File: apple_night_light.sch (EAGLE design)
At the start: 46 parts, among them Y1 16MHZ, Y2 16mhz

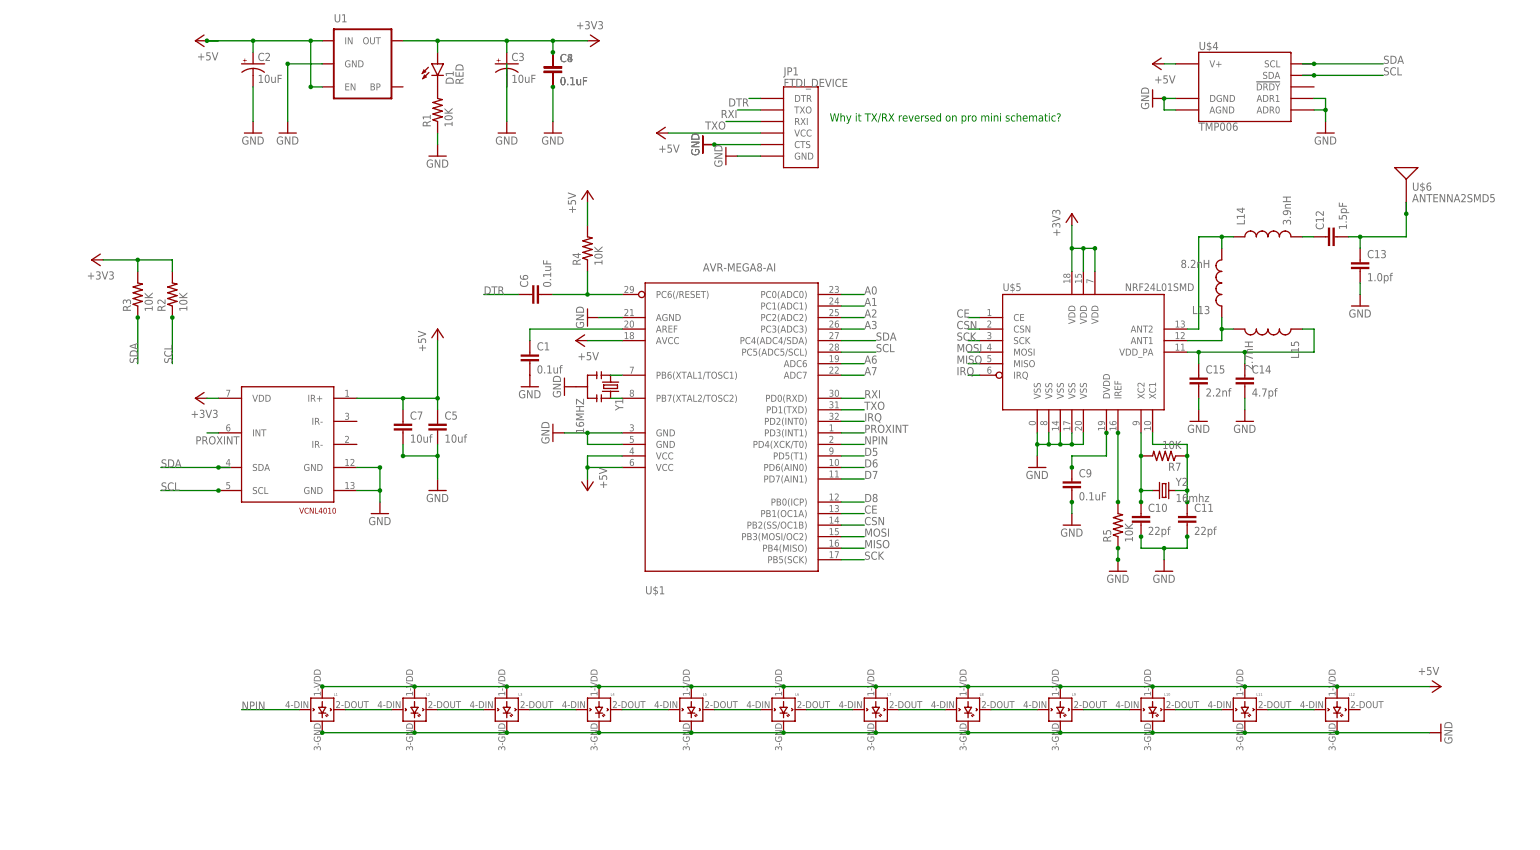
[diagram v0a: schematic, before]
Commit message: some routing, adding current sensor, ground pours
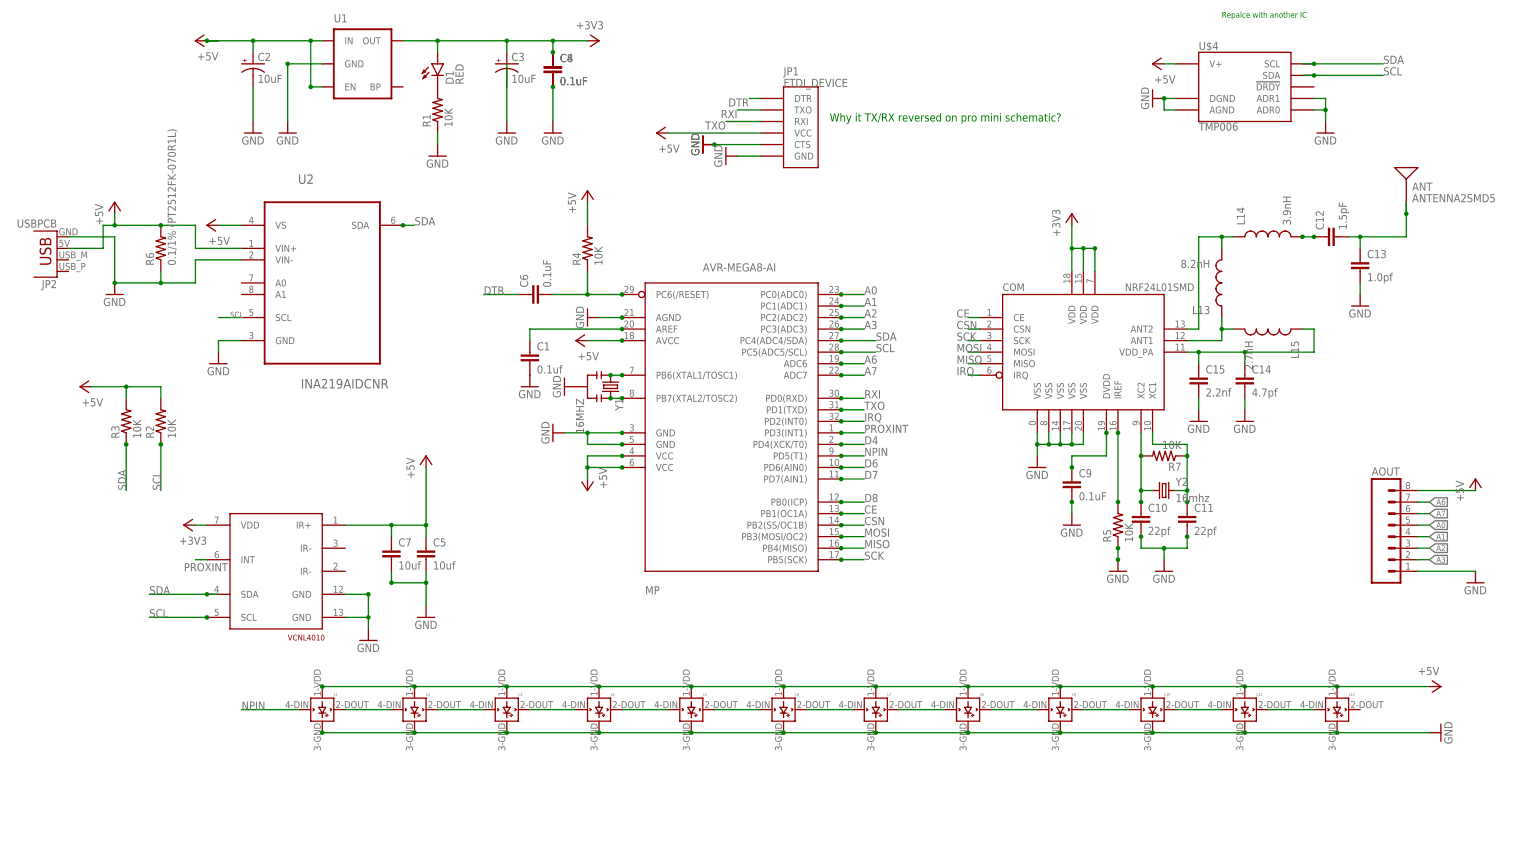
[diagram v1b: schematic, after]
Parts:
- added AOUT: (no value), SparkFun-Connectors:M08NO_SILK
- added JP2: USBPCB, SparkFun-Connectors:USBPCB
- added R6: 0.1/1% (PT2512FK-070R1L), SparkFun-Resistors:RESISTOR2512
- added U2: INA219AIDCNR, Texas Instruments_By_element14_Batch_1:INA219AIDCNR
- renumbered U$1 to MP, U$5 to COM, U$6 to ANT
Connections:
- removed net D5: MP.PD5(T1)
- new net D4: MP.PD4(XCK/T0)
- net +3V3: no longer R2.2, R3.2
- net +5V: now also AOUT.8, JP2.VBUS, R2.2, R3.2, R6.2, U2.VIN+, U2.VS
- net A0: now also AOUT.5
- net A1: now also AOUT.4
- net A2: now also AOUT.3
- net A3: now also AOUT.2
- net A6: now also AOUT.7
- net A7: now also AOUT.6
- net GND: now also AOUT.1, JP2.GND, R6.1, U2.GND, U2.VIN-
- net NPIN: now also MP.PD5(T1); no longer MP.PD4(XCK/T0)
- net PROXINT: now also MP.PD3(INT1)
- net SCL: now also U2.SCL
- net SDA: now also MP.PC4(ADC4/SDA), U2.SDA
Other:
- note added: "Repalce with another IC"
- moved on the sheet: C5, C7, R2, R3

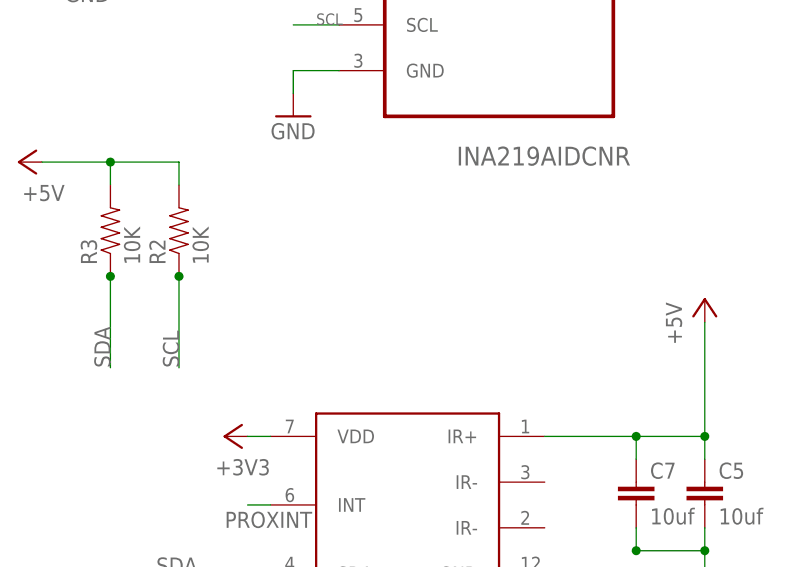
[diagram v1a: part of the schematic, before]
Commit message: usb passthrough placed, better routing on neopixel power
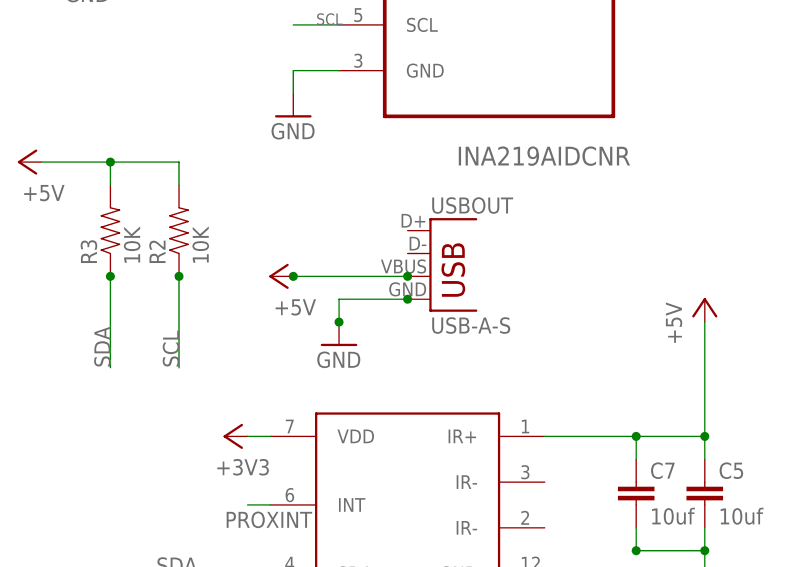
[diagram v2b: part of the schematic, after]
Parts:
- added USBOUT: USB-A-S, SparkFun-Connectors:USB-A-S
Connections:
- net +5V: now also USBOUT.VBUS
- net GND: now also USBOUT.GND
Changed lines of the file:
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@@
 <part name="P+12" library="supply1" deviceset="+5V" device=""/>
 <part name="GND27" library="supply1" deviceset="GND" device=""/>
+<part name="USBOUT" library="SparkFun-Connectors" deviceset="USB" device="-A-S"/>
+<part name="P+13" library="supply1" deviceset="+5V" device=""/>
+<part name="GND28" library="supply1" deviceset="GND" device=""/>
 </parts>
 <sheets>
@@
 <instance part="P+12" gate="1" x="-132.08" y="104.14"/>
 <instance part="GND27" gate="1" x="-132.08" y="83.82"/>
+<instance part="USBOUT" gate="G$1" x="-93.98" y="48.26"/>
+<instance part="P+13" gate="1" x="-111.76" y="50.8" rot="R90"/>
+<instance part="GND28" gate="1" x="-104.14" y="43.18"/>
 </instances>
 <busses>
@@
 <junction x="-132.08" y="99.06"/>
 </segment>
+<segment>
+<wire x1="-96.52" y1="50.8" x2="-109.22" y2="50.8" width="0.1524" layer="91"/>
+<pinref part="P+13" gate="1" pin="+5V"/>
+<pinref part="USBOUT" gate="G$1" pin="VBUS"/>
+<junction x="-96.52" y="50.8"/>
+<junction x="-109.22" y="50.8"/>
+</segment>
 </net>
 <net name="GND" class="0">
@@
 <junction x="-132.08" y="86.36"/>
 </segment>
+<segment>
+<pinref part="USBOUT" gate="G$1" pin="GND"/>
+<wire x1="-96.52" y1="48.26" x2="-104.14" y2="48.26" width="0.1524" layer="91"/>
+<pinref part="GND28" gate="1" pin="GND"/>
+<wire x1="-104.14" y1="48.26" x2="-104.14" y2="45.72" width="0.1524" layer="91"/>
+<junction x="-96.52" y="48.26"/>
+<junction x="-104.14" y="45.72"/>
+</segment>
 </net>

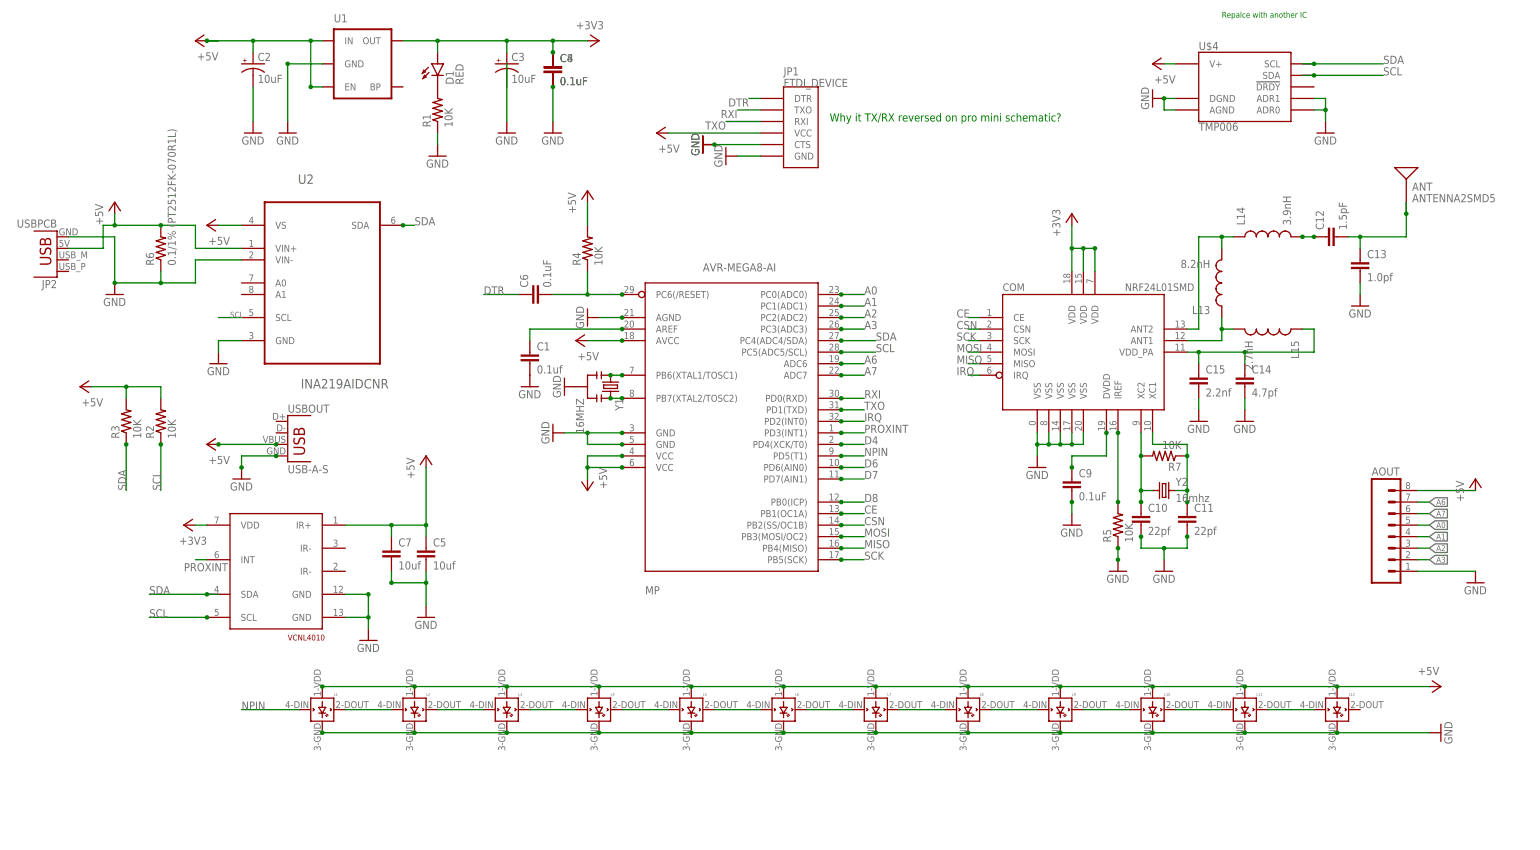
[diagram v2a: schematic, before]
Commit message: moved and corrected currentsensor, trying to fix clearances, adding temp/humidity sensor
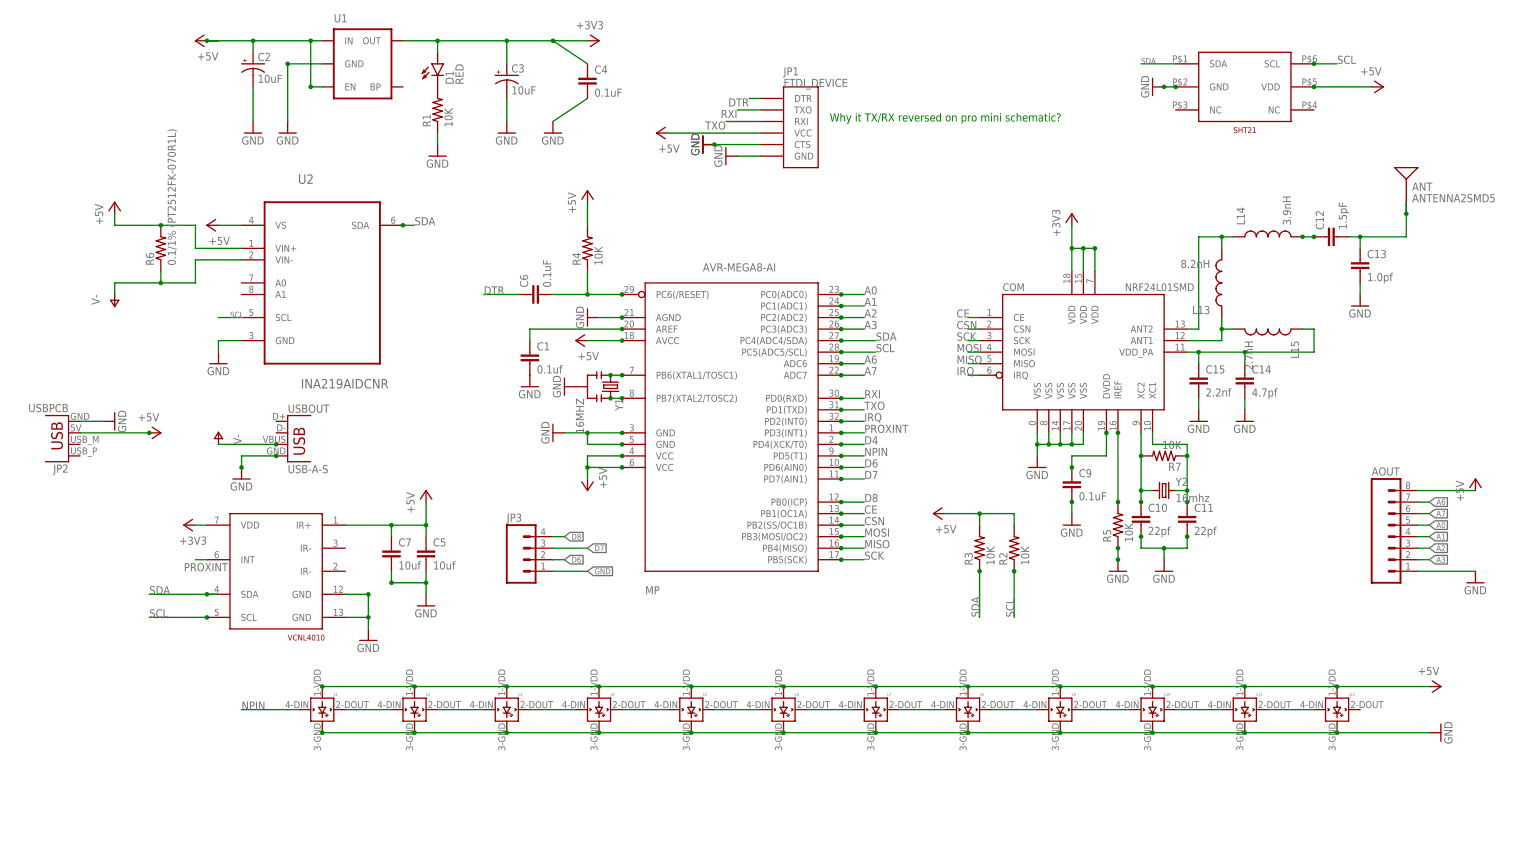
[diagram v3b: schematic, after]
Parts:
- removed C8: 0.1uF, SparkFun-Capacitors:0.1UF-25V(+80/-20%)(0603)
- removed U$4: TMP006, SparkFun-DigitalIC:TMP006
- added JP3: (no value), SparkFun-Connectors:M04LOCK
- added U$1: SHT21, samuel:SHT21
- AOUT: device SparkFun-Connectors:M08NO_SILK -> SparkFun-Connectors:M08LOCK
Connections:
- new net V-: R6.1, U2.VIN-, USBOUT.VBUS
- net +3V3: no longer C8.1
- net +5V: now also U$1.VDD; no longer U$4.V+, USBOUT.VBUS
- net D6: now also JP3.2
- net D7: now also JP3.3
- net D8: now also JP3.4
- net GND: now also JP3.1, U$1.GND; no longer C8.2, R6.1, U$4.ADR0, U$4.ADR1, U$4.AGND, U$4.DGND, U2.VIN-
- net SCL: now also U$1.SCL; no longer U$4.SDA
- net SDA: now also U$1.SDA; no longer U$4.SCL
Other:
- note removed: "Repalce with another IC"
- moved on the sheet: C3, C4, JP2, R2, R3

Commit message: before removing the nrf chip for breakout board
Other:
- moved on the sheet: C4
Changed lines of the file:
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@@
 <part name="JP1" library="SparkFun-Connectors" deviceset="FTDI_DEVICE" device=""/>
 <part name="GND13" library="supply1" deviceset="GND" device=""/>
-<part name="GND14" library="supply1" deviceset="GND" device=""/>
 <part name="P+6" library="supply1" deviceset="+5V" device=""/>
 <part name="GND15" library="supply1" deviceset="GND" device=""/>
@@
 <instance part="C3" gate="G$1" x="-45.72" y="132.08"/>
 <instance part="GND10" gate="1" x="-45.72" y="119.38"/>
-<instance part="C4" gate="G$1" x="-27.94" y="129.54"/>
+<instance part="C4" gate="G$1" x="-35.56" y="127"/>
 <instance part="GND11" gate="1" x="-35.56" y="119.38"/>
 <instance part="+3V2" gate="G$1" x="-116.84" y="33.02" rot="R90"/>
@@
 <instance part="GND12" gate="1" x="-63.5" y="15.24"/>
 <instance part="JP1" gate="G$1" x="15.24" y="121.92"/>
-<instance part="GND13" gate="1" x="2.54" y="114.3" rot="R270"/>
-<instance part="GND14" gate="1" x="-2.54" y="116.84" rot="R270"/>
+<instance part="GND13" gate="1" x="7.62" y="111.76"/>
 <instance part="P+6" gate="1" x="-12.7" y="119.38" rot="R90"/>
-<instance part="GND15" gate="1" x="-2.54" y="116.84" rot="R270"/>
+<instance part="GND15" gate="1" x="0" y="114.3"/>
 <instance part="GND16" gate="1" x="96.52" y="129.54" rot="R270"/>
 <instance part="P+7" gate="1" x="147.32" y="129.54" rot="R270"/>
@@
 <pinref part="GND11" gate="1" pin="GND"/>
 <pinref part="C4" gate="G$1" pin="2"/>
-<wire x1="-35.56" y1="121.92" x2="-27.94" y2="127" width="0.1524" layer="91"/>
+<wire x1="-35.56" y1="121.92" x2="-35.56" y2="124.46" width="0.1524" layer="91"/>
 </segment>
 <segment>
@@
 <segment>
 <pinref part="JP1" gate="G$1" pin="GND"/>
-<wire x1="10.16" y1="114.3" x2="5.08" y2="114.3" width="0.1524" layer="91"/>
+<wire x1="10.16" y1="114.3" x2="7.62" y2="114.3" width="0.1524" layer="91"/>
 <pinref part="GND13" gate="1" pin="GND"/>
 </segment>
@@
 <pinref part="JP1" gate="G$1" pin="CTS"/>
 <wire x1="10.16" y1="116.84" x2="0" y2="116.84" width="0.1524" layer="91"/>
-<pinref part="GND14" gate="1" pin="GND"/>
 <pinref part="GND15" gate="1" pin="GND"/>
-<junction x="0" y="116.84"/>
 </segment>
 <segment>
@@
 <junction x="-45.72" y="139.7"/>
 <pinref part="C4" gate="G$1" pin="1"/>
-<wire x1="-27.94" y1="134.62" x2="-35.56" y2="139.7" width="0.1524" layer="91"/>
+<wire x1="-35.56" y1="132.08" x2="-35.56" y2="139.7" width="0.1524" layer="91"/>
 <junction x="-35.56" y="139.7"/>
 </segment>

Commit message: more stuff, adding crypto board
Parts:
- removed ANT: ANTENNA2SMD5, SparkFun-RF:ANTENNA2SMD5
- removed C10, C11: 22pf, SparkFun-Capacitors:0.1UF-25V(+80/-20%)(0603)
- removed C12: 1.5pF, SparkFun-Capacitors:0.1UF-25V(+80/-20%)(0603)
- removed C13: 1.0pf, SparkFun-Capacitors:0.1UF-25V(+80/-20%)(0603)
- removed C14: 4.7pf, SparkFun-Capacitors:0.1UF-25V(+80/-20%)(0603)
- removed C15: 2.2nf, SparkFun-Capacitors:0.1UF-25V(+80/-20%)(0603)
- removed C9: 0.1uF, SparkFun-Capacitors:0.1UF-25V(+80/-20%)(0603)
- removed COM: NRF24L01SMD, SparkFun-RF:NRF24L01SMD
- removed L13: 8.2nH, SparkFun-Passives:INDUCTOR0402
- removed L14: 3.9nH, SparkFun-Passives:INDUCTOR0402
- removed L15: 2.7nH, SparkFun-Passives:INDUCTOR0402
- removed R5, R7: 10K, SparkFun-Resistors:10KOHM-1/10W-1%(0603)0603
- removed Y2: 16mhz, SparkFun-FreqCtrl:CRYSTAL5X3
- added NRF: M04X2, SparkFun-Connectors:M04X2
- added SPI: AVR_SPI_PRG_6NS, SparkFun-Connectors:AVR_SPI_PRG_6NS
- added U3: ATSHA204-TSU, SparkFun-DigitalIC:ATSHA204-TSU
- renumbered JP3 to DOUT
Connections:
- removed net N$1: C14.1, C15.1, COM.VDD_PA, L15.1
- removed net N$15: C9.1, COM.DVDD
- removed net N$26: COM.ANT2, L13.2, L14.1
- removed net N$27: C10.1, COM.XC2, R7.2, Y2.1
- removed net N$30: C11.1, COM.XC1, R7.1, Y2.2
- removed net N$31: C12.1, L14.2
- removed net N$32: ANT.SIGNAL, C12.2, C13.1
- removed net N$6: COM.ANT1, L13.1, L15.2
- removed net N$8: COM.IREF, R5.2
- net +3V3: now also NRF.2; no longer COM.VDD@15, COM.VDD@18, COM.VDD@7
- net +5V: now also SPI.2, U3.VCC
- net CE: now also NRF.3; no longer COM.CE
- net CSN: now also NRF.4, SPI.5; no longer COM.CSN
- net GND: now also NRF.1, SPI.6, U$3.IR-@1, U$3.IR-@2, U3.GND; no longer C10.2, C11.2, C13.2, C14.2, C15.2, C9.2, COM.VSS@0, COM.VSS@14, COM.VSS@17, COM.VSS@20, COM.VSS@8, R5.1
- net IRQ: now also NRF.8; no longer COM.IRQ
- net MISO: now also NRF.7, SPI.1; no longer COM.MISO
- net MOSI: now also NRF.6, SPI.4; no longer COM.MOSI
- net SCK: now also NRF.5, SPI.3; no longer COM.SCK
- net SDA: now also U3.SDA
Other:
- moved on the sheet: R4
